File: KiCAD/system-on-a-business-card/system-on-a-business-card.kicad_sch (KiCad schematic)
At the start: 15 parts, among them J1 USB_C_Receptacle, J3 Conn_01x04_Socket, SW1 SW_Push, U1 USBLC6-2SC6

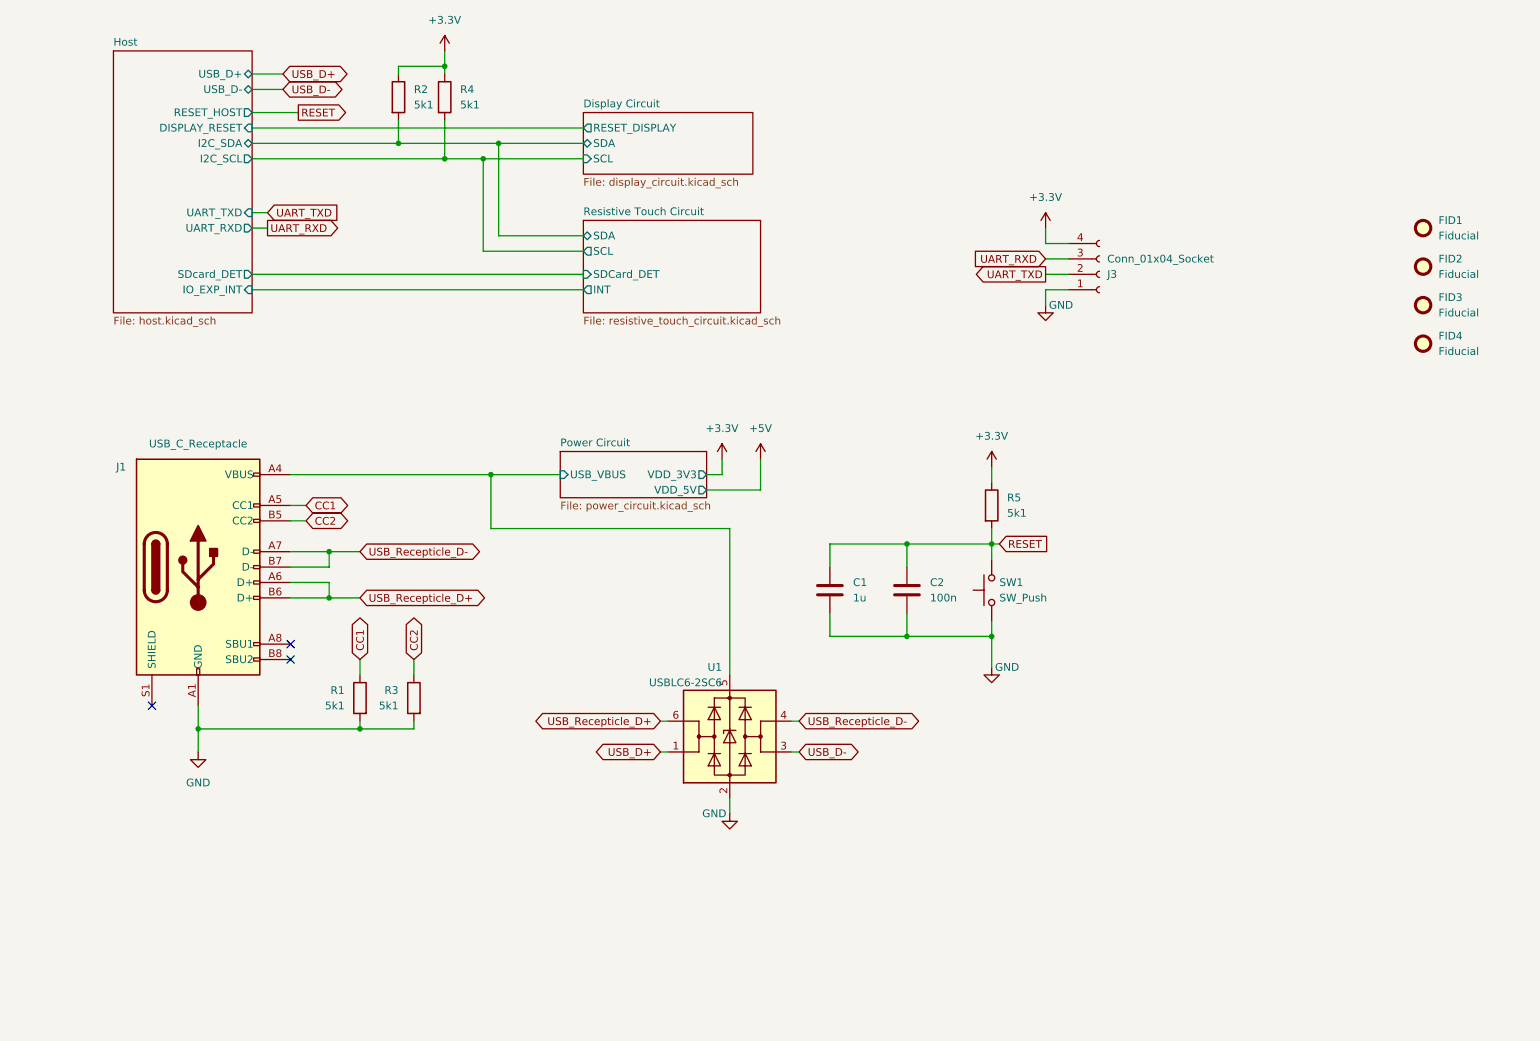
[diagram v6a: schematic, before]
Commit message: #10: connected display reset to GPIO Expander
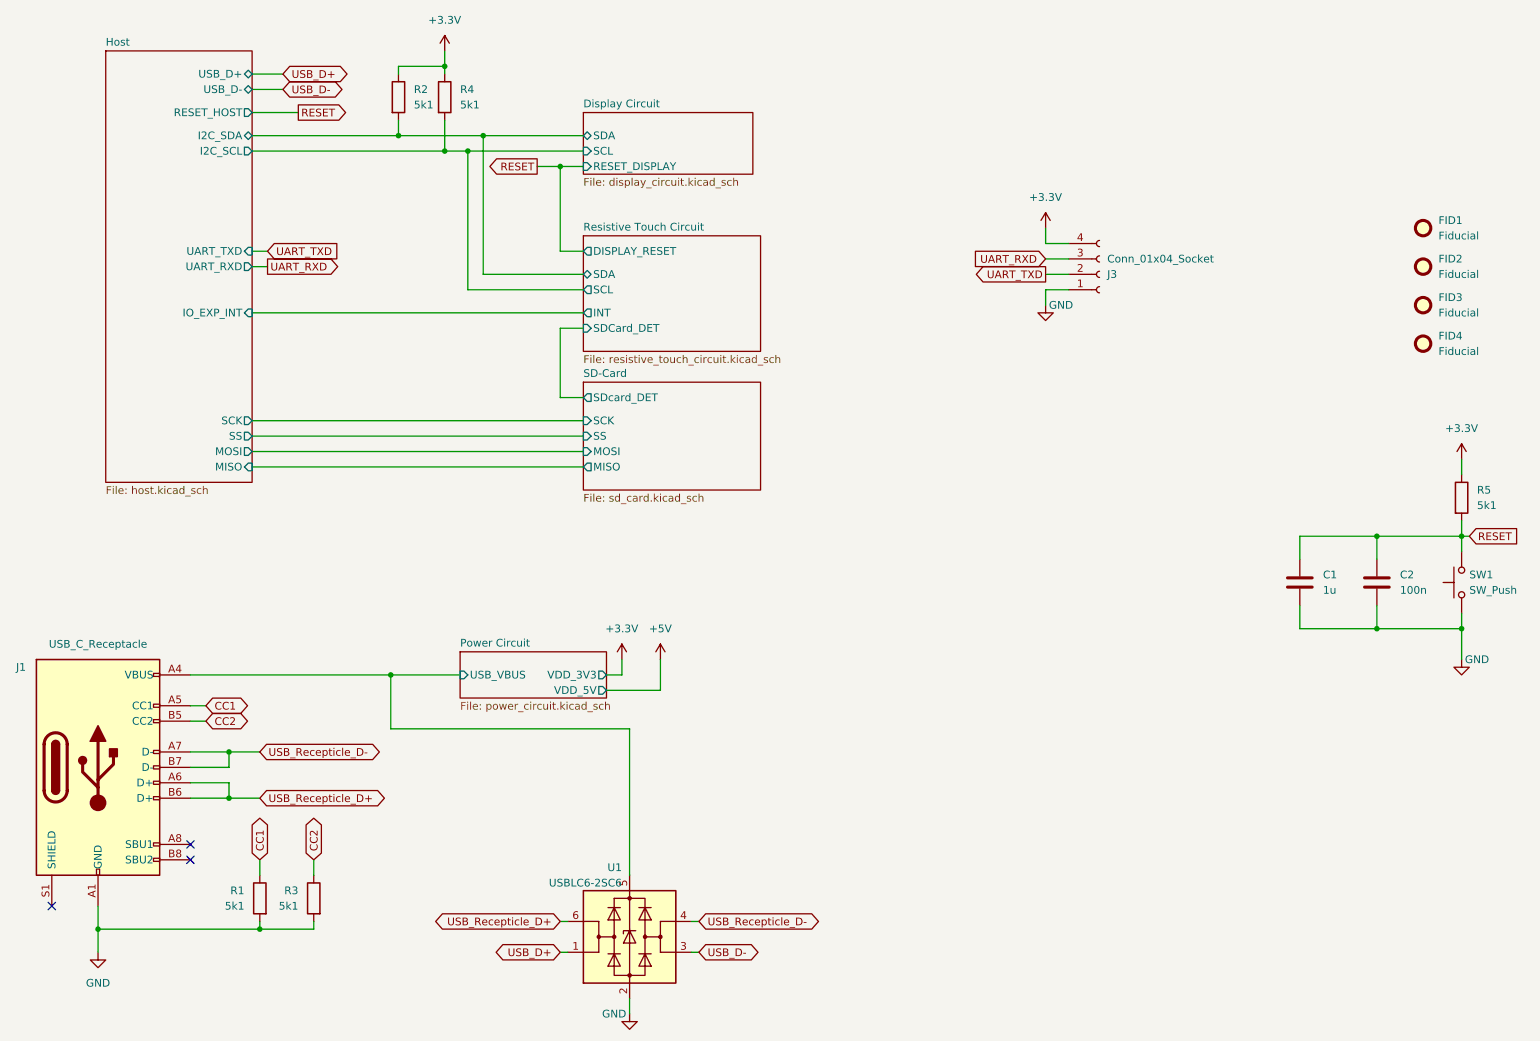
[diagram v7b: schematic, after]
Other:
- added sheet SD-Card (sd_card.kicad_sch)
- sheet Host ports: added MISO, MOSI, SCK, SS; removed DISPLAY_RESET, SDcard_DET
- sheet Resistive Touch Circuit ports: added DISPLAY_RESET; removed none
- moved on the sheet: C1, C2, J1, R1, R3, R5, SW1, U1

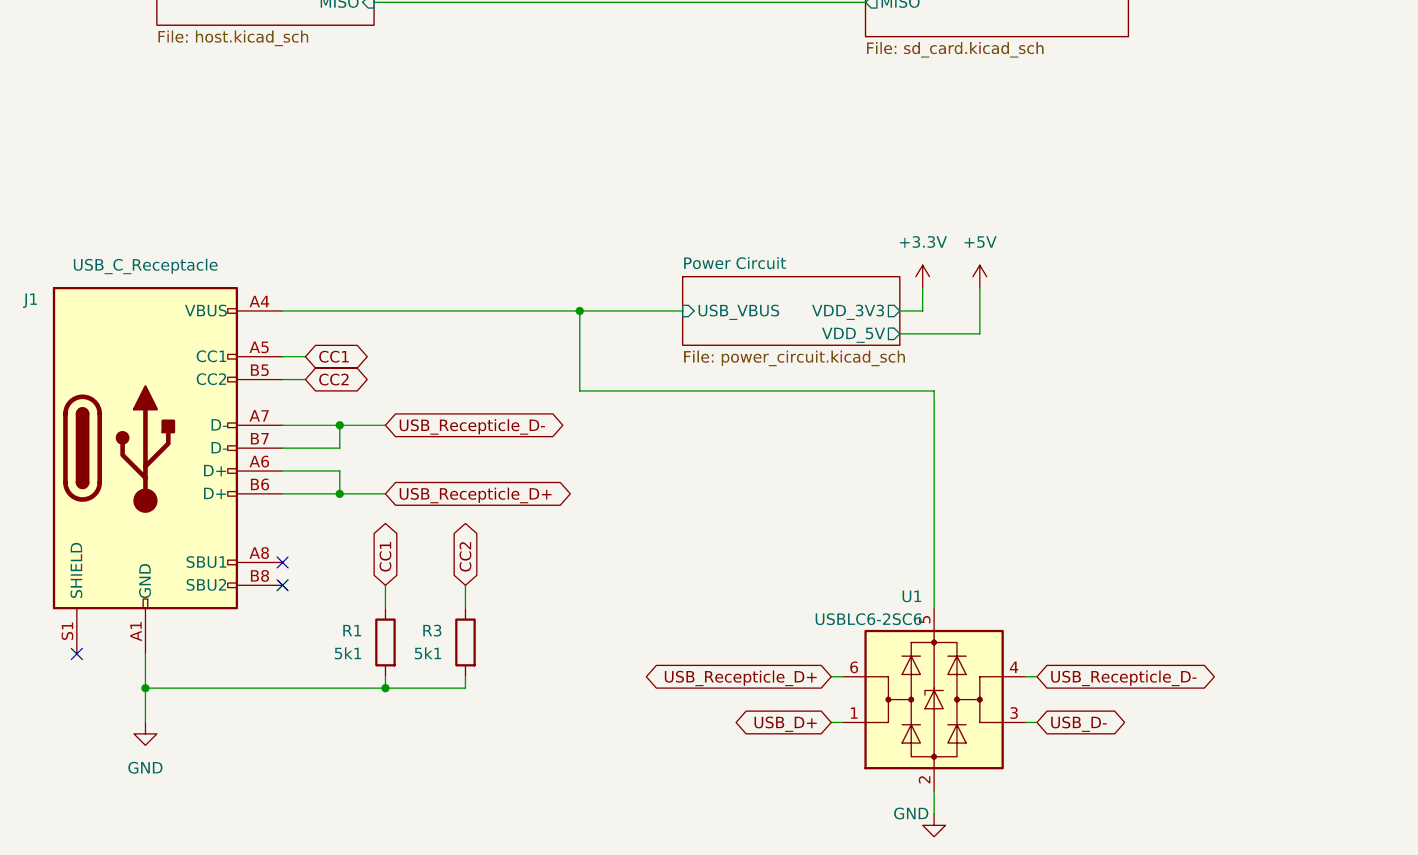
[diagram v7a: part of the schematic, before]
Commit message: #10: mintor tweaks in routing, removed fiducials from bom, added values to buzzer and sd-card slot
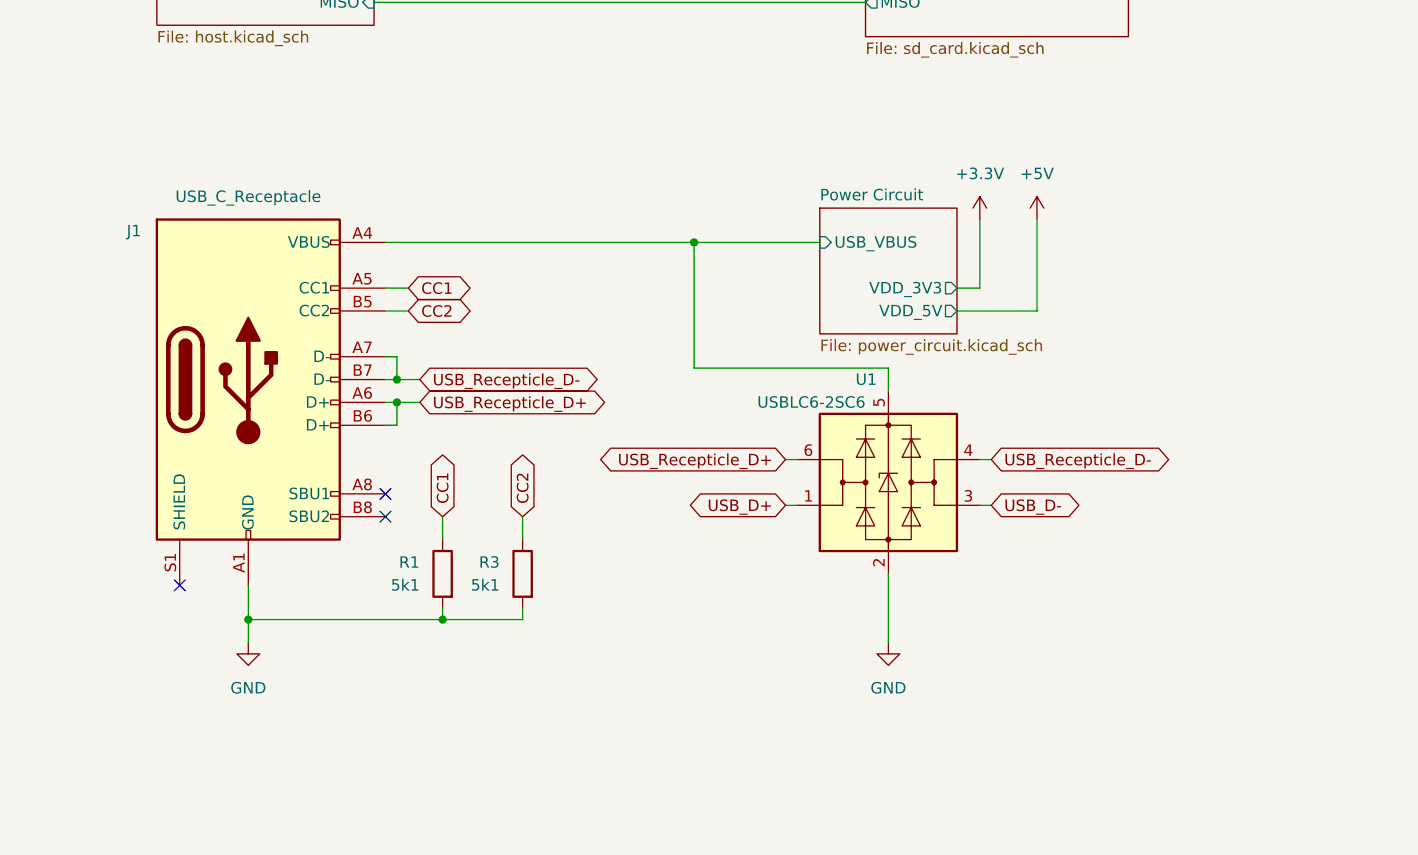
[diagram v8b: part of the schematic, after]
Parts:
- FID1, FID2, FID3, FID4: now left out of the parts list
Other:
- moved on the sheet: J1, R1, R3, U1
